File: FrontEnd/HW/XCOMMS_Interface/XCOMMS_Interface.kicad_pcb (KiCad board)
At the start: 4 copper layers, 40 x 65 mm, 98 parts, among them J1 TFC-110-02-F-D-A-P-FR, U1 STM32L4, U10 TPS784, U11 AD5160, U12 TPS56637RPAR, U13 MAX870EUK, U14 MAX870EUK, U15 MAX870EUK, U16 TPS56637RPAR, U17 INA290, U9 TPS56637RPAR, Y1 TCXO 10 MHz

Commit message: Altium to KiCad translation of interface board
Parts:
- removed 12 V: MOLEX_52610271, 3CAT_Connectors.PcbLib:532610271
- removed the JTAG at (154.1, 74.7)
- removed the UART at (142.9, 74.7)
- added 12V: MOLEX_52610271, Connector_Molex:Molex_PicoBlade_53261-0271_1x02-1MP_P1.25mm_Horizontal, F.Cu at (148.4, 134.4)
- added Designator10: Comment, D:_GoogleDrive_UPC_MEE_IR_Altium_Library_Altium_libraries_3CAT_Official_lib_3C4_OFFICIAL_LIB.PcbLib_PCB_ID, F.Cu at (144.3, 112.5)
- added JTAG: MOLEX_532610471, Connector_Molex:Molex_PicoBlade_53261-0471_1x04-1MP_P1.25mm_Horizontal, F.Cu at (154.1, 75.7)
- added UART: MOLEX_532610471, Connector_Molex:Molex_PicoBlade_53261-0471_1x04-1MP_P1.25mm_Horizontal, F.Cu at (142.7, 75.7)
- C1: renamed from C2; value Cap Semi -> 4.7uF; footprint Miscellaneous_GGS.PcbLib:0805 SMD Capacitor -> Capacitor_SMD:C_0805_2012Metric
- C10: renamed from C68; value Cap Semi -> 10uF; footprint Miscellaneous_GGS.PcbLib:0805 SMD Capacitor -> Capacitor_SMD:C_0805_2012Metric
- C11: renamed from C69; value Cap Semi -> 10uF; footprint Miscellaneous_GGS.PcbLib:0805 SMD Capacitor -> Capacitor_SMD:C_0805_2012Metric
- C12: renamed from C70; value Cap Semi -> 100nF; footprint Miscellaneous_GGS.PcbLib:0603 SMD Capacitor -> Capacitor_SMD:C_0603_1608Metric
- C13: renamed from C84; value Cap Semi -> 10uF; footprint Miscellaneous_GGS.PcbLib:0805 SMD Capacitor -> Capacitor_SMD:C_0805_2012Metric
- C14: renamed from C85; value Cap Semi -> 10uF; footprint Miscellaneous_GGS.PcbLib:0805 SMD Capacitor -> Capacitor_SMD:C_0805_2012Metric
- C15: renamed from C86; value Cap Semi -> 100nF; footprint Miscellaneous_GGS.PcbLib:0603 SMD Capacitor -> Capacitor_SMD:C_0603_1608Metric
- C16: renamed from C62; value Cap Semi -> 100nF; footprint Miscellaneous_GGS.PcbLib:0603 SMD Capacitor -> Capacitor_SMD:C_0603_1608Metric
- C17: renamed from C77; value Cap Semi -> 100nF; footprint Miscellaneous_GGS.PcbLib:0603 SMD Capacitor -> Capacitor_SMD:C_0603_1608Metric
- C18: renamed from C87; value Cap Semi -> 100nF; footprint Miscellaneous_GGS.PcbLib:0603 SMD Capacitor -> Capacitor_SMD:C_0603_1608Metric
- C19: renamed from C63; value Cap Semi -> 10uF; footprint Miscellaneous_GGS.PcbLib:0805 SMD Capacitor -> Capacitor_SMD:C_0805_2012Metric
- C2: renamed from C1; value Cap Semi -> 1uF; footprint Miscellaneous_GGS.PcbLib:0603 SMD Capacitor -> Capacitor_SMD:C_0603_1608Metric
- C20: renamed from C81; value Cap Semi -> 10uF; footprint Miscellaneous_GGS.PcbLib:0805 SMD Capacitor -> Capacitor_SMD:C_0805_2012Metric
- C21: renamed from C88; value Cap Semi -> 10uF; footprint Miscellaneous_GGS.PcbLib:0805 SMD Capacitor -> Capacitor_SMD:C_0805_2012Metric
- C22: renamed from C67; value Cap Semi -> 10uF; footprint Miscellaneous_GGS.PcbLib:0805 SMD Capacitor -> Capacitor_SMD:C_0805_2012Metric
- C23: renamed from C83; value Cap Semi -> 10uF; footprint Miscellaneous_GGS.PcbLib:0805 SMD Capacitor -> Capacitor_SMD:C_0805_2012Metric
- C24: renamed from C90; value Cap Semi -> 10uF; footprint Miscellaneous_GGS.PcbLib:0805 SMD Capacitor -> Capacitor_SMD:C_0805_2012Metric
- C25: renamed from C64; value Cap Semi -> 100pF; footprint Miscellaneous_GGS.PcbLib:0603 SMD Capacitor -> Capacitor_SMD:C_0603_1608Metric
- C26: renamed from C82; value Cap Semi -> 100pF; footprint Miscellaneous_GGS.PcbLib:0603 SMD Capacitor -> Capacitor_SMD:C_0603_1608Metric
- C27: renamed from C89; value Cap Semi -> 100pF; footprint Miscellaneous_GGS.PcbLib:0603 SMD Capacitor -> Capacitor_SMD:C_0603_1608Metric
- C28: renamed from C7; value Cap Semi -> 100nF; footprint Miscellaneous_GGS.PcbLib:0603 SMD Capacitor -> Capacitor_SMD:C_0603_1608Metric
- C29: renamed from C78; value Cap Semi -> 0.33uF; footprint Miscellaneous_GGS.PcbLib:0603 SMD Capacitor -> Capacitor_SMD:C_0603_1608Metric
- C3, C4, C6: value Cap Semi -> 100nF; footprint Miscellaneous_GGS.PcbLib:0603 SMD Capacitor -> Capacitor_SMD:C_0603_1608Metric
- C30: renamed from C61; value Cap Semi -> 1uF; footprint Miscellaneous_GGS.PcbLib:0603 SMD Capacitor -> Capacitor_SMD:C_0603_1608Metric
- C31: renamed from C65; value Cap Semi -> 1uF; footprint Miscellaneous_GGS.PcbLib:0603 SMD Capacitor -> Capacitor_SMD:C_0603_1608Metric
- C32: renamed from C66; value Cap Semi -> 1uF; footprint Miscellaneous_GGS.PcbLib:0603 SMD Capacitor -> Capacitor_SMD:C_0603_1608Metric
- C33: renamed from C71; value Cap Semi -> 0.33uF; footprint Miscellaneous_GGS.PcbLib:0603 SMD Capacitor -> Capacitor_SMD:C_0603_1608Metric
- C34: renamed from C74; value Cap Semi -> 0.33uF; footprint Miscellaneous_GGS.PcbLib:0603 SMD Capacitor -> Capacitor_SMD:C_0603_1608Metric
- C35: renamed from C79; value Cap Semi -> 0.33uF; footprint Miscellaneous_GGS.PcbLib:0603 SMD Capacitor -> Capacitor_SMD:C_0603_1608Metric
- C36: renamed from C72; value Cap Semi -> 0.33uF; footprint Miscellaneous_GGS.PcbLib:0603 SMD Capacitor -> Capacitor_SMD:C_0603_1608Metric
- C37: renamed from C75; value Cap Semi -> 0.33uF; footprint Miscellaneous_GGS.PcbLib:0603 SMD Capacitor -> Capacitor_SMD:C_0603_1608Metric
- C38: renamed from C80; value Cap Semi -> 0.33uF; footprint Miscellaneous_GGS.PcbLib:0603 SMD Capacitor -> Capacitor_SMD:C_0603_1608Metric
- C39: renamed from C73; value Cap Semi -> 0.33uF; footprint Miscellaneous_GGS.PcbLib:0603 SMD Capacitor -> Capacitor_SMD:C_0603_1608Metric
- C40: renamed from C76; value Cap Semi -> 0.33uF; footprint Miscellaneous_GGS.PcbLib:0603 SMD Capacitor -> Capacitor_SMD:C_0603_1608Metric
- C5: value Cap Semi -> 1uF; footprint Miscellaneous_GGS.PcbLib:0603 SMD Capacitor -> Capacitor_SMD:C_0603_1608Metric
- C7: renamed from C58; value Cap Semi -> 10uF; footprint Miscellaneous_GGS.PcbLib:0805 SMD Capacitor -> Capacitor_SMD:C_0805_2012Metric
- C8: renamed from C59; value Cap Semi -> 10uF; footprint Miscellaneous_GGS.PcbLib:0805 SMD Capacitor -> Capacitor_SMD:C_0805_2012Metric
- C9: renamed from C60; value Cap Semi -> 100nF; footprint Miscellaneous_GGS.PcbLib:0603 SMD Capacitor -> Capacitor_SMD:C_0603_1608Metric
- J1: footprint Connectors_GGS.PcbLib:SAMTEC_TFC-110-02-F-D-A-P-FR -> GGS_Connectors:SAMTEC_TFC-110-02-F-D-A-P-FR
- L1: renamed from L3; value 652-SRP5030T-3R3M -> 3.3uH; footprint Miscellaneous_GGS.PcbLib:Bourns_SRP5030T-3R3M -> Inductor_SMD:L_Bourns_SRP5030T
- L2: renamed from L4; value 652-SRP5030T-3R3M -> 3.3uH; footprint Miscellaneous_GGS.PcbLib:Bourns_SRP5030T-3R3M -> Inductor_SMD:L_Bourns_SRP5030T
- L3: renamed from L5; value WE_74438356022 -> 2.2uH; footprint Miscellaneous_GGS.PcbLib:Coilcraft_XAL60xx -> Inductor_SMD:L_Coilcraft_XAL60xx_6.36x6.56mm
- R1: value Res3 -> 510; footprint Miscellaneous_GGS.PcbLib:0603 SMD Resistor -> Resistor_SMD:R_0603_1608Metric
- R10: renamed from R12; value Res3 -> 10k; footprint Miscellaneous_GGS.PcbLib:0603 SMD Resistor -> Resistor_SMD:R_0603_1608Metric
- R11: renamed from R18; value Res3 -> 10k; footprint Miscellaneous_GGS.PcbLib:0603 SMD Resistor -> Resistor_SMD:R_0603_1608Metric
- R12: renamed from R29; value Res3 -> 10k; footprint Miscellaneous_GGS.PcbLib:0603 SMD Resistor -> Resistor_SMD:R_0603_1608Metric
- R13: renamed from R19; value Res3 -> 10k; footprint Miscellaneous_GGS.PcbLib:0603 SMD Resistor -> Resistor_SMD:R_0603_1608Metric
- R14: renamed from R17; value Res3 -> 0R; footprint Miscellaneous_GGS.PcbLib:0603 SMD Resistor -> Resistor_SMD:R_0603_1608Metric
- R15: renamed from R24; value Res3 -> 20k; footprint Miscellaneous_GGS.PcbLib:0603 SMD Resistor -> Resistor_SMD:R_0603_1608Metric
- R16: renamed from R20; value Res3 -> 10k; footprint Miscellaneous_GGS.PcbLib:0603 SMD Resistor -> Resistor_SMD:R_0603_1608Metric
- R17: renamed from R25; value Res3 -> 20k; footprint Miscellaneous_GGS.PcbLib:0603 SMD Resistor -> Resistor_SMD:R_0603_1608Metric
- R18: renamed from R14; value Res3 -> 20k; footprint Miscellaneous_GGS.PcbLib:0603 SMD Resistor -> Resistor_SMD:R_0603_1608Metric
- R19: renamed from R15; value Res3 -> 5k; footprint Miscellaneous_GGS.PcbLib:0603 SMD Resistor -> Resistor_SMD:R_0603_1608Metric
- R2: renamed from R27; value Res3 -> 169k; footprint Miscellaneous_GGS.PcbLib:0603 SMD Resistor -> Resistor_SMD:R_0603_1608Metric
- R20: renamed from R21; value Res3 -> 10k; footprint Miscellaneous_GGS.PcbLib:0603 SMD Resistor -> Resistor_SMD:R_0603_1608Metric
- R21: renamed from R26; value Res3 -> 20k; footprint Miscellaneous_GGS.PcbLib:0603 SMD Resistor -> Resistor_SMD:R_0603_1608Metric
- R3: renamed from R13; value Res3 -> 90.9k; footprint Miscellaneous_GGS.PcbLib:0603 SMD Resistor -> Resistor_SMD:R_0603_1608Metric
- R4: renamed from R16; value Res3 -> 20k; footprint Miscellaneous_GGS.PcbLib:0603 SMD Resistor -> Resistor_SMD:R_0603_1608Metric
- R5: renamed from R22; value Res3 -> 73.2k; footprint Miscellaneous_GGS.PcbLib:0603 SMD Resistor -> Resistor_SMD:R_0603_1608Metric
- R6: renamed from R23; value Res3 -> 20k; footprint Miscellaneous_GGS.PcbLib:0603 SMD Resistor -> Resistor_SMD:R_0603_1608Metric
- R7: renamed from R30; value Res3 -> 45.3k; footprint Miscellaneous_GGS.PcbLib:0603 SMD Resistor -> Resistor_SMD:R_0603_1608Metric
- R8: renamed from R31; value Res3 -> 20k; footprint Miscellaneous_GGS.PcbLib:0603 SMD Resistor -> Resistor_SMD:R_0603_1608Metric
- R9: renamed from R28; value Res3 -> 36.1k; footprint Miscellaneous_GGS.PcbLib:0603 SMD Resistor -> Resistor_SMD:R_0603_1608Metric
- Rsense1, Rsense2: value Res3 -> 0R005; footprint Miscellaneous_GGS.PcbLib:1206 SMD RESISTOR -> Resistor_SMD:R_1206_3216Metric
- SCRW1, SCRW2, SCRW3, SCRW4: value Metric Screw Hole -> MountingHole_Pad; footprint 3CAT_Miscellaneous.PcbLib:M3 ScrewHole -> MountingHole:MountingHole_3.2mm_M3_Pad_Via
- TP1: renamed from TP4; value TP -> TestPoint; footprint Connectors_GGS.PcbLib:TestPoint -> TestPoint:TestPoint_Pad_D1.0mm
- TP2: renamed from TP6; value TP -> TestPoint; footprint Connectors_GGS.PcbLib:TestPoint -> TestPoint:TestPoint_Pad_D1.0mm
- TP3: renamed from TP10; value TP -> TestPoint; footprint Connectors_GGS.PcbLib:TestPoint -> TestPoint:TestPoint_Pad_D1.0mm
- TP4: renamed from TP7; value TP -> TestPoint; footprint Connectors_GGS.PcbLib:TestPoint -> TestPoint:TestPoint_Pad_D1.0mm
- TP5: value TP -> TestPoint; footprint Connectors_GGS.PcbLib:TestPoint -> TestPoint:TestPoint_Pad_D1.0mm
- TP6: renamed from TP8; value TP -> TestPoint; footprint Connectors_GGS.PcbLib:TestPoint -> TestPoint:TestPoint_Pad_D1.0mm
- TP7: renamed from TP9; value TP -> TestPoint; footprint Connectors_GGS.PcbLib:TestPoint -> TestPoint:TestPoint_Pad_D1.0mm
- U1: value STM32L4 -> STM32L431KBUx; footprint Miscellaneous_GGS.PcbLib:QFN-33N -> Package_DFN_QFN:QFN-32-1EP_5x5mm_P0.5mm_EP3.45x3.45mm
- U10: renamed from U15; footprint Power_GGS.PcbLib:SOT23-5N -> Package_TO_SOT_SMD:SOT-23-5
- U2: renamed from U9; value TPS56637RPAR -> TPS56637; footprint Power_GGS.PcbLib:CONV_TPS56637RPAR -> GGS_Power:TPS56637RPAR
- U3: renamed from U12; value TPS56637RPAR -> TPS56637; footprint Power_GGS.PcbLib:CONV_TPS56637RPAR -> GGS_Power:TPS56637RPAR
- U4: renamed from U16; value TPS56637RPAR -> TPS56637; footprint Power_GGS.PcbLib:CONV_TPS56637RPAR -> GGS_Power:TPS56637RPAR
- U5: renamed from U10; footprint Power_GGS.PcbLib:SOT23-5N -> Package_TO_SOT_SMD:SOT-23-5
- U6: renamed from U13; footprint Power_GGS.PcbLib:SOT23-5N -> Package_TO_SOT_SMD:SOT-23-5
- U7: renamed from U17; footprint Miscellaneous_GGS.PcbLib:SC70-5 -> GGS_Miscellaneous:SC70-5
- U8: renamed from U11; footprint Miscellaneous_GGS.PcbLib:SOT-28-8N -> Package_TO_SOT_SMD:SOT-23-8
- U9: renamed from U14; footprint Power_GGS.PcbLib:SOT23-5N -> Package_TO_SOT_SMD:SOT-23-5
- Y1: value TCXO 10 MHz -> TCXO_ECS; footprint Miscellaneous_GGS.PcbLib:ECS-TXO-2016 -> GGS_Miscellaneous:TCXO_ECS
- moved U3 5.25 mm to (138.7, 115.7)
- moved U4 5.12 mm to (161.9, 115.9)
- moved Y1 5.07 mm to (160.6, 92.7)
- moved U7 5.00 mm to (154.9, 109.8)
- moved U2 5.00 mm to (149.9, 116.0)
- moved R9 1.55 mm to (158.0, 124.0), turned to 0 degrees
- moved TP5 0.94 mm to (148.6, 96.5)
- moved TP7 0.71 mm to (133.6, 100.3)
- moved TP4 0.71 mm to (133.6, 86.6)
- moved TP6 0.70 mm to (133.6, 93.3)
- moved R14 0.49 mm to (147.8, 94.7)
- moved C12 0.44 mm to (138.4, 123.7)
- moved R7 0.37 mm to (157.2, 116.8)
- moved R8 0.36 mm to (155.7, 116.8), turned to -90 degrees
- moved L3 0.34 mm to (161.8, 114.8)
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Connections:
- net 5V_EN renamed /5V_EN
- net 6V_EN renamed /6V_EN
- net CurrentSense renamed /CurrentSense
- net LO_EN renamed /LO_EN
- net NetC65_1 renamed Net-(C31-Pad1)
- net NetR27_2 renamed Net-(R2-Pad2)
- net PLL_CSB renamed /PLL_CSB
- net R_CSB renamed /R_CSB
- net SCK renamed /SCK
- net SDI renamed /SDI
- net SDO renamed /SDO
- net T_CSB renamed /T_CSB
- net Tx_CE renamed /Tx_CE
- net Tx_PM renamed /Tx_PM
- net Vd_PA renamed /Vd_PA
- net mcu_OSC renamed /mcu_OSC
- C1 pad 1: GND -> +3V3
- C1 pad 2: 3V3 -> GND
- C10 pad 1: GND -> +12V
- C10 pad 2: 12V -> GND
- C11 pad 1: GND -> +12V
- C11 pad 2: 12V -> GND
- C12 pad 1: 12V -> +12V
- C13 pad 1: GND -> +12V
- C13 pad 2: 12V -> GND
- C14 pad 1: GND -> +12V
- C14 pad 2: 12V -> GND
- C15 pad 1: 12V -> +12V
- C16 pad 1: NetC62_1 -> Net-(C16-Pad1)
- C16 pad 2: NetC62_2 -> Net-(C16-Pad2)
- C17 pad 1: NetC77_1 -> Net-(C17-Pad1)
- C17 pad 2: NetC77_2 -> Net-(C17-Pad2)
- C18 pad 1: NetC87_1 -> Net-(C18-Pad1)
- C18 pad 2: NetC87_2 -> Net-(C18-Pad2)
- C19 pad 1: GND -> /XCOMMS_PowerSupply/6V
- C19 pad 2: 6V -> GND
- C2 pad 1: GND -> +3V3
- C2 pad 2: 3V3 -> GND
- C20 pad 1: GND -> +5V
- C20 pad 2: 5V -> GND
- C21 pad 1: GND -> +3V3
- C21 pad 2: 3V3 -> GND
- C22 pad 1: GND -> /XCOMMS_PowerSupply/6V
- C22 pad 2: 6V -> GND
- C23 pad 1: GND -> +5V
- C23 pad 2: 5V -> GND
- C24 pad 1: GND -> +3V3
- C24 pad 2: 3V3 -> GND
- C25 pad 1: NetC64_1 -> Net-(C25-Pad1)
- C25 pad 2: NetC64_2 -> Net-(C25-Pad2)
- C26 pad 1: NetC82_1 -> Net-(C26-Pad1)
- C26 pad 2: NetC82_2 -> Net-(C26-Pad2)
- C27 pad 1: NetC89_1 -> Net-(C27-Pad1)
- C27 pad 2: NetC89_2 -> Net-(C27-Pad2)
- C28 pad 1: 5V -> GND
- C28 pad 2: GND -> +5V
- C29 pad 1: NetC78_1 -> GND
- C29 pad 2: GND -> Net-(C29-Pad2)
- C3 pad 1: 3V3 -> +3V3
- C30 pad 1: 3V3 -> +3V3
- C33 pad 1: Vinv_in -> GND
- C33 pad 2: GND -> /XCOMMS_PowerSupply/Vinv_in
- C34 pad 1: NetC74_1 -> Net-(C34-Pad1)
- C34 pad 2: NetC74_2 -> Net-(C34-Pad2)
- C35 pad 1: NetC79_1 -> GND
- C35 pad 2: GND -> Net-(C35-Pad2)
- C36 pad 1: Vinv_in -> GND
- C36 pad 2: GND -> /XCOMMS_PowerSupply/Vinv_in
- C37 pad 1: NetC75_1 -> Net-(C37-Pad1)
- C37 pad 2: NetC75_2 -> Net-(C37-Pad2)
- C38 pad 1: NetC80_1 -> GND
- C38 pad 2: GND -> Net-(C38-Pad2)
- C39 pad 1: Vinv_in -> GND
- C39 pad 2: GND -> /XCOMMS_PowerSupply/Vinv_in
- C4 pad 1: 3V3 -> +3V3
- C40 pad 1: NetC76_1 -> Net-(C40-Pad1)
- C40 pad 2: NetC76_2 -> Net-(C40-Pad2)
- C5 pad 1: GND -> +3V3
- C5 pad 2: 3V3 -> GND
- C6 pad 1: 3V3 -> +3V3
- C7 pad 1: GND -> +12V
- C7 pad 2: 12V -> GND
- C8 pad 1: GND -> +12V
- C8 pad 2: 12V -> GND
- C9 pad 1: 12V -> +12V
- J1 pad 01: 5V -> +5V
- J1 pad 02: 3V3 -> +3V3
- J1 pad 16: Vg_PA3 -> /Vg_PA3
- J1 pad 18: Vg_PA2 -> /Vg_PA2
- J1 pad 20: Vg_PA1 -> /Vg_PA1
- L1 pad 1: NetC62_1 -> Net-(C16-Pad2)
- L1 pad 2: 6V -> /XCOMMS_PowerSupply/6V
- L2 pad 1: NetC77_1 -> Net-(C17-Pad2)
- L2 pad 2: 5V -> +5V
- L3 pad 1: NetC87_1 -> Net-(C18-Pad2)
- L3 pad 2: 3V3 -> +3V3
- R1 pad 1: GND -> /Boot0
- R1 pad 2: NetR1_2 -> GND
- R10 pad 1: NetC64_2 -> Net-(C25-Pad1)
- R11 pad 1: NetC82_2 -> Net-(C26-Pad1)
- R12 pad 1: NetC89_2 -> Net-(C27-Pad1)
- R13 pad 1: NetC78_1 -> Net-(C29-Pad2)
- R13 pad 2: Vg_PA1 -> /Vg_PA1
- R14 pad 2: Vinv_in -> /XCOMMS_PowerSupply/Vinv_in
- R15 pad 1: GND -> /Vg_PA1
- R15 pad 2: Vg_PA1 -> GND
- R16 pad 1: NetC79_1 -> Net-(C35-Pad2)
- R16 pad 2: Vg_PA2 -> /Vg_PA2
- R17 pad 1: GND -> /Vg_PA2
- R17 pad 2: Vg_PA2 -> GND
- R18 pad 1: NetR14_1 -> Net-(R18-Pad1)
- R18 pad 2: NetR14_2 -> Net-(R18-Pad2)
- R19 pad 1: GND -> Net-(R18-Pad2)
- R19 pad 2: NetR14_1 -> GND
- R2 pad 1: 12V -> +12V
- R20 pad 1: NetC80_1 -> Net-(C38-Pad2)
- R20 pad 2: Vg_PA3 -> /Vg_PA3
- R21 pad 1: GND -> /Vg_PA3
- R21 pad 2: Vg_PA3 -> GND
- R3 pad 1: NetC64_2 -> /XCOMMS_PowerSupply/6V
- R3 pad 2: 6V -> Net-(C25-Pad1)
- R4 pad 1: NetC64_1 -> /XCOMMS_PowerSupply/6V
- R4 pad 2: 6V -> Net-(C25-Pad2)
- R5 pad 1: 5V -> +5V
- R5 pad 2: NetC82_2 -> Net-(C26-Pad1)
- R6 pad 1: NetC82_1 -> +5V
- R6 pad 2: 5V -> Net-(C26-Pad2)
- R7 pad 1: 3V3 -> +3V3
- R7 pad 2: NetC89_2 -> Net-(C27-Pad1)
- R8 pad 1: NetC89_1 -> +3V3
- R8 pad 2: 3V3 -> Net-(C27-Pad2)
- Rsense1 pad 1: 6V -> /XCOMMS_PowerSupply/6V
- Rsense2 pad 1: 6V -> /XCOMMS_PowerSupply/6V
- TP1 pad 1: 6V -> /XCOMMS_PowerSupply/6V
- TP2 pad 1: 5V -> +5V
- TP3 pad 1: 3V3 -> +3V3
- TP4 pad 1: Vg_PA1 -> /Vg_PA1
- TP6 pad 1: Vg_PA2 -> /Vg_PA2
- TP7 pad 1: Vg_PA3 -> /Vg_PA3
- U1 pad 1: 3V3 -> +3V3
- U1 pad 17: 3V3 -> +3V3
- U1 pad 18: USART1_CK -> unconnected-(U1-Pad18)
- U1 pad 19: USART1_Tx -> /USART1_Tx
- U1 pad 2: (no net) -> unconnected-(U1-Pad2)
- U1 pad 20: USART1_Rx -> /USART1_Rx
- U1 pad 21: USART1_CTS -> /USART1_CTS
- U1 pad 22: (no net) -> unconnected-(U1-Pad22)
- U1 pad 23: JTMS -> /JTMS
- U1 pad 24: JTCK -> /JTCK
- U1 pad 25: JTDI -> /JTDI
- U1 pad 26: JTDO -> /JTDO
- U1 pad 3: (no net) -> unconnected-(U1-Pad3)
- U1 pad 31: NetR1_2 -> /Boot0
- U1 pad 4: (no net) -> unconnected-(U1-Pad4)
- U1 pad 5: 3V3 -> +3V3
- U1 pad 9: (no net) -> unconnected-(U1-Pad9)
- U10 pad 1: NetC80_1 -> Net-(C38-Pad2)
- U10 pad 2: Vinv_in -> /XCOMMS_PowerSupply/Vinv_in
- U10 pad 3: NetC76_2 -> Net-(C40-Pad1)
- U10 pad 5: NetC76_1 -> Net-(C40-Pad2)
- U2 pad 2: NetC64_2 -> Net-(C25-Pad1)
- U2 pad 4: (no net) -> unconnected-(U2-Pad4)
- U2 pad 5: (no net) -> unconnected-(U2-Pad5)
- U2 pad 6: NetC62_1 -> Net-(C16-Pad2)
- U2 pad 7: NetC62_2 -> Net-(C16-Pad1)
- U2 pad 8: 12V -> +12V
- U3 pad 2: NetC82_2 -> Net-(C26-Pad1)
- U3 pad 4: (no net) -> unconnected-(U3-Pad4)
- U3 pad 5: (no net) -> unconnected-(U3-Pad5)
- U3 pad 6: NetC77_1 -> Net-(C17-Pad2)
- U3 pad 7: NetC77_2 -> Net-(C17-Pad1)
- U3 pad 8: 12V -> +12V
- U4 pad 2: NetC89_2 -> Net-(C27-Pad1)
- U4 pad 4: (no net) -> unconnected-(U4-Pad4)
- U4 pad 5: (no net) -> unconnected-(U4-Pad5)
- U4 pad 6: NetC87_1 -> Net-(C18-Pad2)
- U4 pad 7: NetC87_2 -> Net-(C18-Pad1)
- U4 pad 8: 12V -> +12V
- U5 pad 1: 3V3 -> +3V3
- U5 pad 3: 3V3 -> +3V3
- U5 pad 4: NetR14_2 -> Net-(R18-Pad1)
- U6 pad 1: NetC78_1 -> Net-(C29-Pad2)
- U6 pad 2: Vinv_in -> /XCOMMS_PowerSupply/Vinv_in
- U6 pad 3: NetC74_2 -> Net-(C34-Pad1)
- U6 pad 5: NetC74_1 -> Net-(C34-Pad2)
- U7 pad 3: 5V -> +5V
- U7 pad 4: 6V -> /XCOMMS_PowerSupply/6V
- U8 pad 2: 3V3 -> unconnected-(U8-Pad2)
- U8 pad 7: NetR14_2 -> Net-(R18-Pad1)
- U8 pad 8: (no net) -> unconnected-(U8-Pad8)
- U9 pad 1: NetC79_1 -> Net-(C35-Pad2)
- U9 pad 2: Vinv_in -> /XCOMMS_PowerSupply/Vinv_in
- U9 pad 3: NetC75_2 -> Net-(C37-Pad1)
- U9 pad 5: NetC75_1 -> Net-(C37-Pad2)
- Y1 pad 1: 3V3 -> +3V3
- Y1 pad 4: 3V3 -> +3V3
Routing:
- net 3V3: track 126.9 -> 0.00 mm, vias 6 -> 0
- net +3V3: track 0.00 -> 121.9 mm, vias 0 -> 6
- net 12V: track 50.6 -> 0.00 mm, vias 1 -> 0
- net 5V: track 50.2 -> 0.00 mm, vias 3 -> 0
- net +12V: track 0.00 -> 49.8 mm, vias 0 -> 1
- net +5V: track 0.00 -> 49.6 mm, vias 0 -> 3
- net Vinv_in: track 31.5 -> 0.00 mm
- net /XCOMMS_PowerSupply/Vinv_in: track 0.00 -> 29.6 mm
- net 6V: track 22.7 -> 0.00 mm
- net Vg_PA1: track 22.3 -> 0.00 mm, vias 2 -> 0
- net /Vg_PA1: track 0.00 -> 21.6 mm, vias 0 -> 2
- net /XCOMMS_PowerSupply/6V: track 0.00 -> 21.5 mm
- net USART1_CK: track 18.0 -> 0.00 mm, vias 1 -> 0
- net Vg_PA2: track 17.0 -> 0.00 mm, vias 2 -> 0
- net USART1_Tx: track 16.5 -> 0.00 mm, vias 1 -> 0
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- added copper zone on B.Cu, net Net-(C16-Pad2)
- added copper zone on B.Cu, net Net-(C17-Pad2)
- added copper zone on B.Cu, net Net-(C18-Pad2)
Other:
- outline, holes or cut-outs redrawn

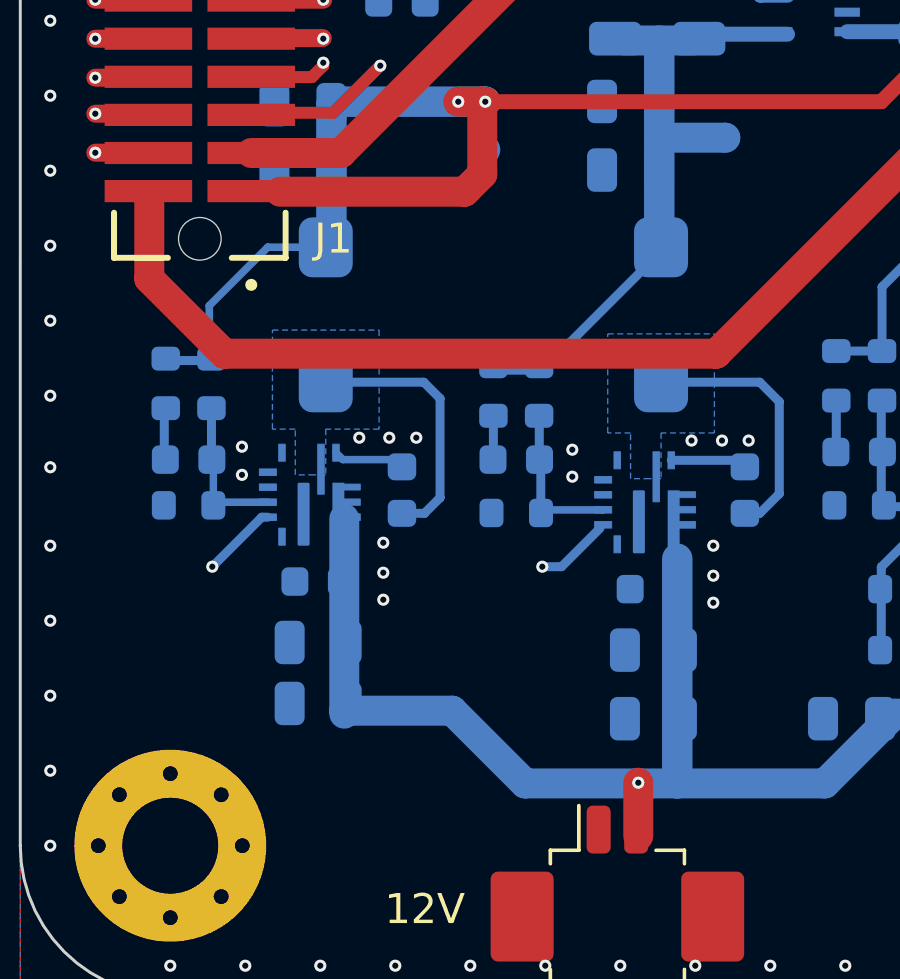
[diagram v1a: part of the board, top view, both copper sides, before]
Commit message: Interface board modified
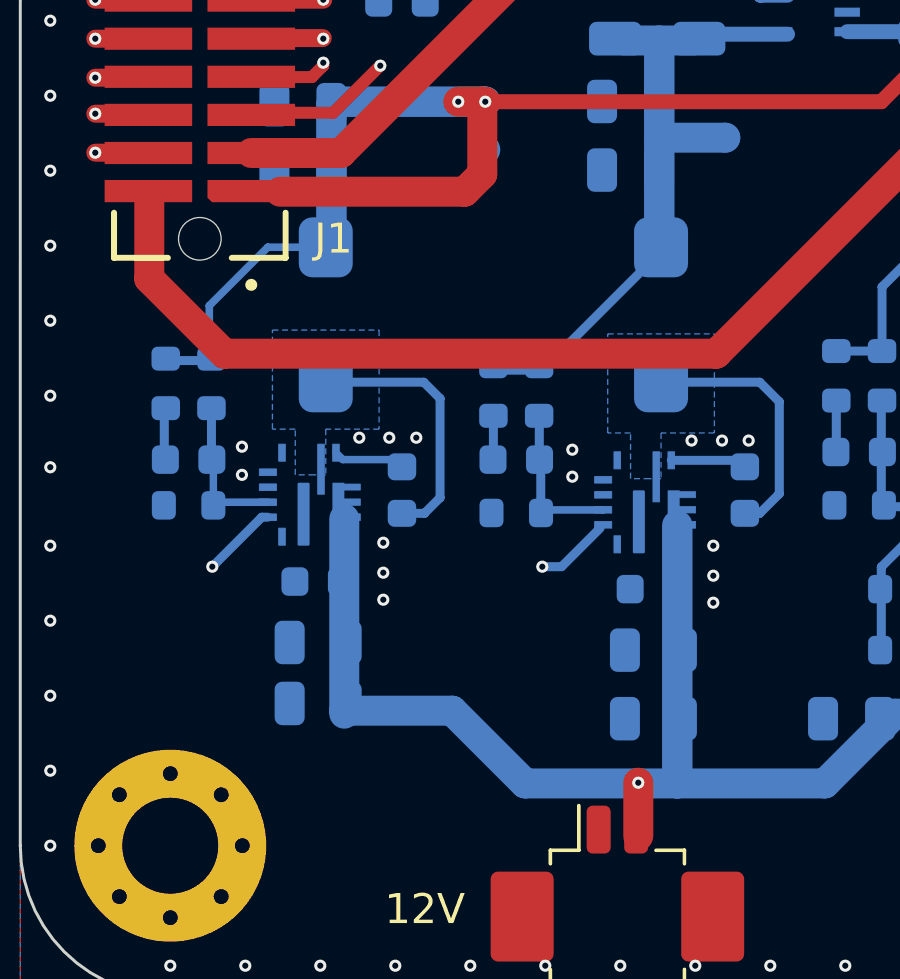
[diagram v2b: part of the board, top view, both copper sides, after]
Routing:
- net +12V: track 49.8 -> 50.9 mm

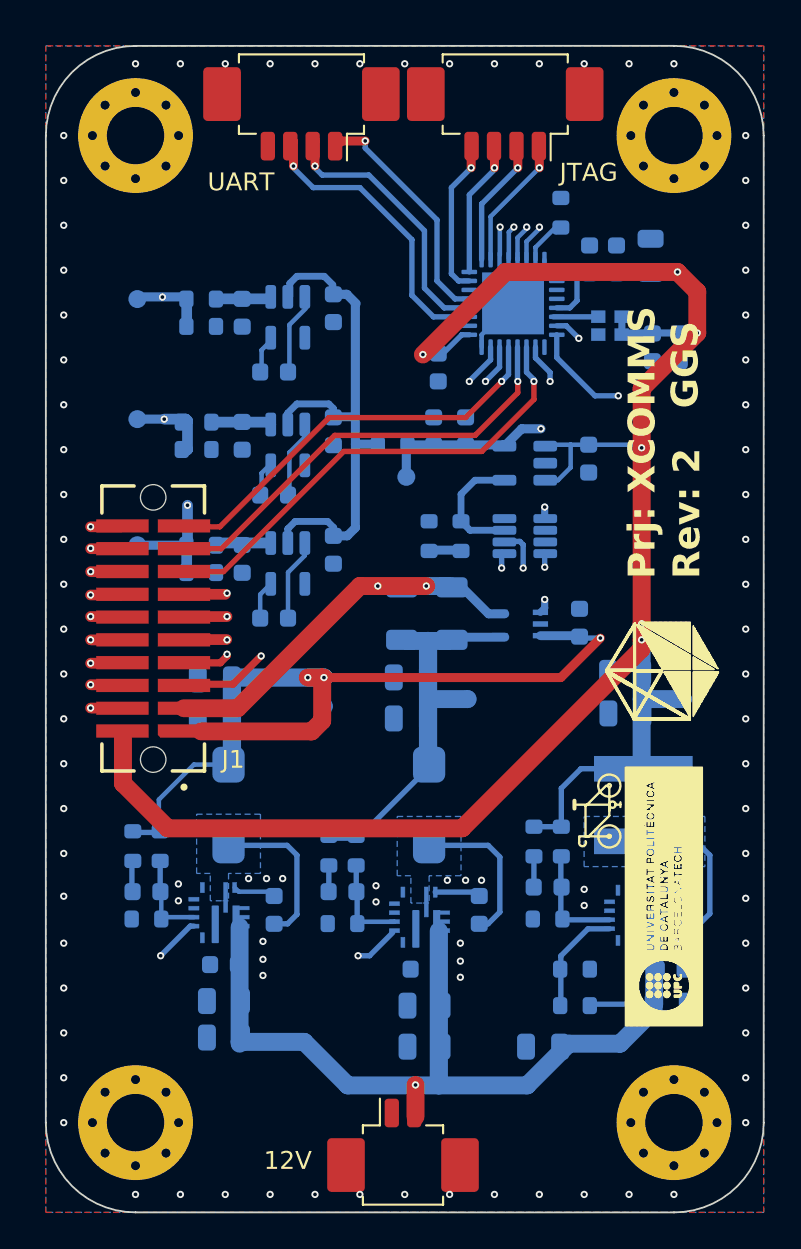
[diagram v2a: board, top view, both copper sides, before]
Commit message: XCOMMS_RF and XCOMMS_Interface KiCad design updated
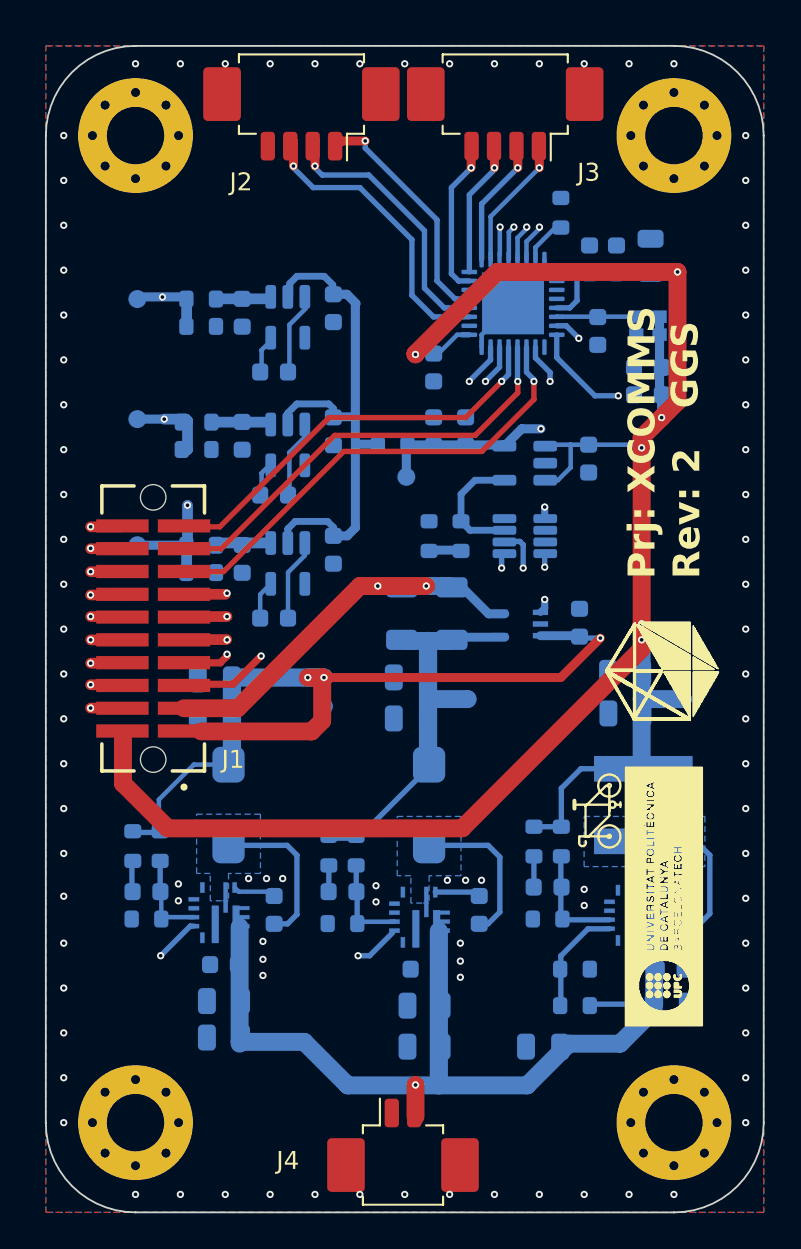
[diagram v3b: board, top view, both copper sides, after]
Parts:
- added C_TCXO1: 100nF, Capacitor_SMD:C_0603_1608Metric, B.Cu at (159.3, 88.4)
- J2: renamed from UART; value MOLEX_532610471 -> UART
- J3: renamed from JTAG; value MOLEX_532610471 -> JTAG
- J4: renamed from 12V; value MOLEX_52610271 -> 12V
- R1: value 510 -> 10k
- moved C5 2.66 mm to (162.1, 91.9), turned to 180 degrees
- moved Y1 2.12 mm to (162.7, 92.7)
- moved C6 2.08 mm to (162.1, 90.4), turned to 180 degrees
- moved C4 0.25 mm to (150.1, 90.4)
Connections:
- net Net-(C16-Pad1) renamed /XCOMMS_PowerSupply/Buck6V_Boot
- net Net-(C16-Pad2) renamed /XCOMMS_PowerSupply/Buck6V_SW
- net Net-(C17-Pad1) renamed /XCOMMS_PowerSupply/Buck5V_Boot
- net Net-(C17-Pad2) renamed /XCOMMS_PowerSupply/Buck5V_SW
- net Net-(C18-Pad1) renamed /XCOMMS_PowerSupply/Buck3V3_Boot
- net Net-(C18-Pad2) renamed /XCOMMS_PowerSupply/Buck3V3_SW
- net Net-(C25-Pad1) renamed /XCOMMS_PowerSupply/Buck6V_FB
- net Net-(C26-Pad1) renamed /XCOMMS_PowerSupply/Buck5V_FB
- net Net-(C27-Pad1) renamed /XCOMMS_PowerSupply/Buck3V3_FB
- net Net-(C27-Pad2) renamed /XCOMMS_PowerSupply/Buck3V3_Comp
- net Net-(C29-Pad2) renamed /XCOMMS_PowerSupply/Inv1_Out
- net Net-(C31-Pad1) renamed /XCOMMS_PowerSupply/LDO_Out
- net Net-(C34-Pad1) renamed /XCOMMS_PowerSupply/Inv_C-
- net Net-(C34-Pad2) renamed /XCOMMS_PowerSupply/Inv_C+
- net Net-(C35-Pad2) renamed /XCOMMS_PowerSupply/Inv2_Out
- net Net-(C37-Pad1) renamed /XCOMMS_PowerSupply/Inv2_C-
- net Net-(C37-Pad2) renamed /XCOMMS_PowerSupply/Inv2_C+
- net Net-(C38-Pad2) renamed /XCOMMS_PowerSupply/Inv3_Out
- net Net-(C40-Pad1) renamed /XCOMMS_PowerSupply/Inv3_C-
- net Net-(C40-Pad2) renamed /XCOMMS_PowerSupply/Inv3_C+
- net Net-(R18-Pad1) renamed /XCOMMS_PowerSupply/LDO_FB
- net Net-(R2-Pad2) renamed /XCOMMS_PowerSupply/Buck3V3_En
- J2 pad 4: unconnected-(UART1-Pad4) -> /USART1_CK
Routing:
- net /mcu_OSC: track 2.53 -> 4.43 mm
- net +3V3: track 121.9 -> 123.0 mm

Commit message: XCOMMS RF update and PA EvalBoard
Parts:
- SCRW1, SCRW2, SCRW3, SCRW4: footprint MountingHole:MountingHole_3.2mm_M3_Pad_Via -> MountingHole:MountingHole_2.7mm_M2.5_Pad
- moved Designator7 40.3 mm to (135.6, 129.6), turned to 0 degrees
- moved Designator6 36.8 mm to (135.5, 127.1), turned to 0 degrees
- moved J2 32.5 mm to (164.8, 99.5), turned to 90 degrees
- moved Designator9 30.6 mm to (135.4, 134.5), turned to 0 degrees
- moved Designator8 28.9 mm to (142.9, 135.6), turned to 0 degrees
- moved J4 18.9 mm to (164.5, 124.5), turned to 90 degrees
- moved J3 14.5 mm to (164.8, 85.5), turned to 90 degrees
- moved SCRW3 3.54 mm to (131.0, 75.0)
- moved SCRW4 2.92 mm to (165.0, 75.0)
- moved SCRW1 2.91 mm to (131.0, 134.0)
- moved SCRW2 2.12 mm to (165.0, 134.0)
- moved C1 0.71 mm to (161.7, 83.7)
- moved C10 0.71 mm to (137.9, 127.3)
- moved C11 0.71 mm to (137.9, 125.2)
- moved C13 0.71 mm to (155.7, 127.8)
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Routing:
- net +12V: track 50.9 -> 49.1 mm, vias 1 -> 0
- net /USART1_CTS: track 13.3 -> 11.7 mm, vias 1 -> 0
- net /JTDI: track 7.34 -> 5.81 mm, vias 1 -> 0
- net /JTDO: track 7.75 -> 6.24 mm, vias 1 -> 0
- net /JTCK: track 7.79 -> 6.28 mm, vias 1 -> 0
- net /JTMS: track 9.03 -> 7.52 mm, vias 1 -> 0
- net /USART1_Tx: track 16.5 -> 15.1 mm, vias 1 -> 0
- net /USART1_Rx: track 15.1 -> 13.7 mm, vias 1 -> 0
- net GND: vias 101 -> 94
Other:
- outline, holes or cut-outs redrawn
